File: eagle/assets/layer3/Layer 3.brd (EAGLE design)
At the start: 196 x 158 mm, 84 parts, among them Q2 AO3402, X1 SM06B-SRSS-TB, Y1 8MHz

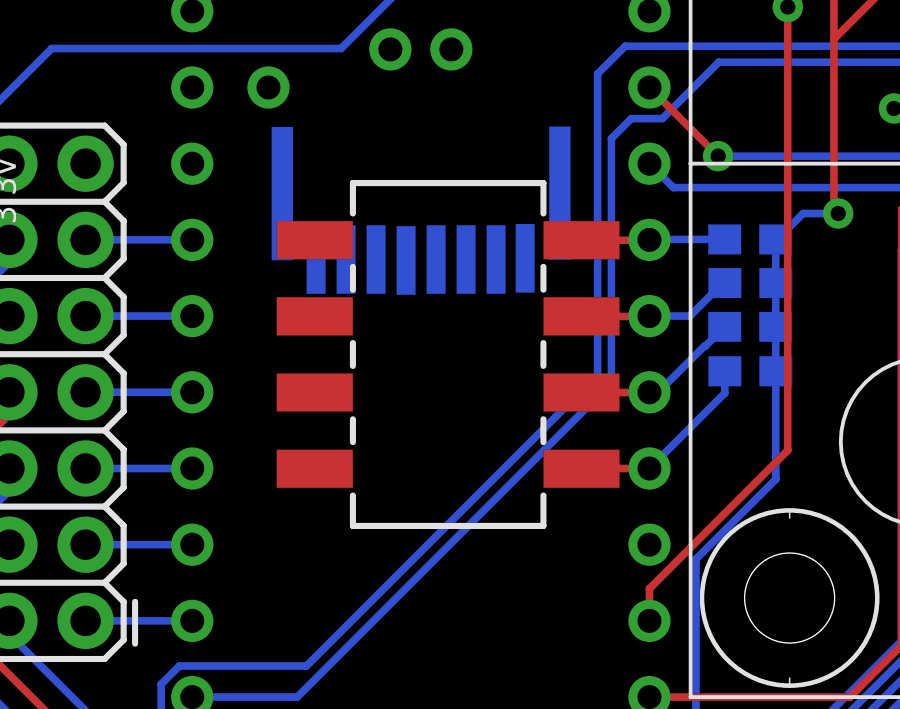
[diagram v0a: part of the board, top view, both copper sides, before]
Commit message: added teensy 4 lbr
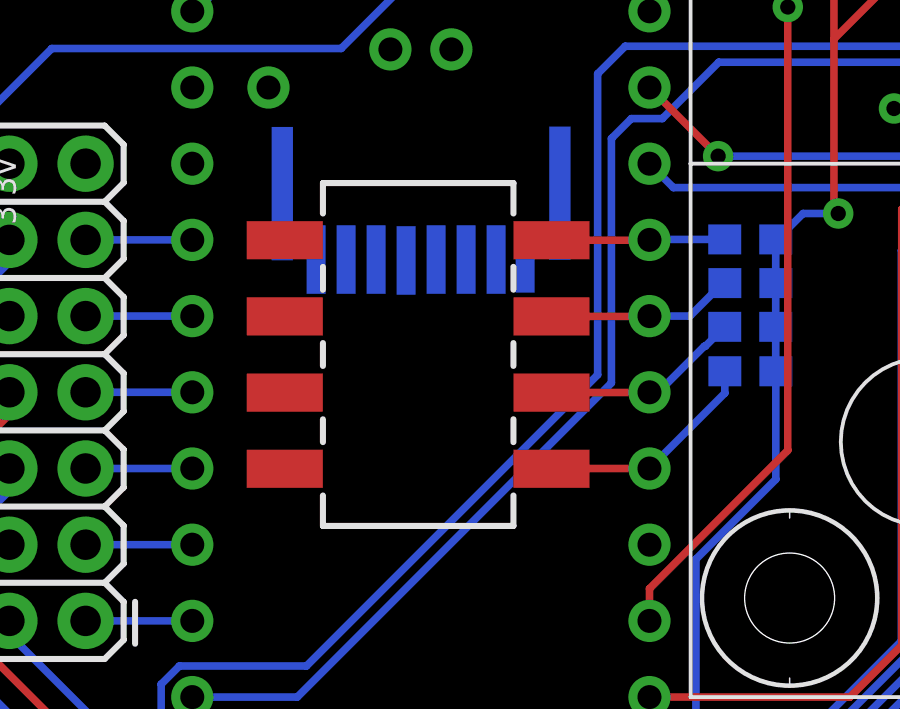
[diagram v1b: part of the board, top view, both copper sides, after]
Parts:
- moved S1 1.00 mm to (-26.9, 3.80)
- renumbered U$1 to TEENSY4
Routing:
- net DIP4: track 6.55 -> 7.55 mm
- net DIP3: track 5.68 -> 6.68 mm
- net DIP2: track 5.24 -> 6.24 mm
- net DIP1: track 4.78 -> 5.78 mm

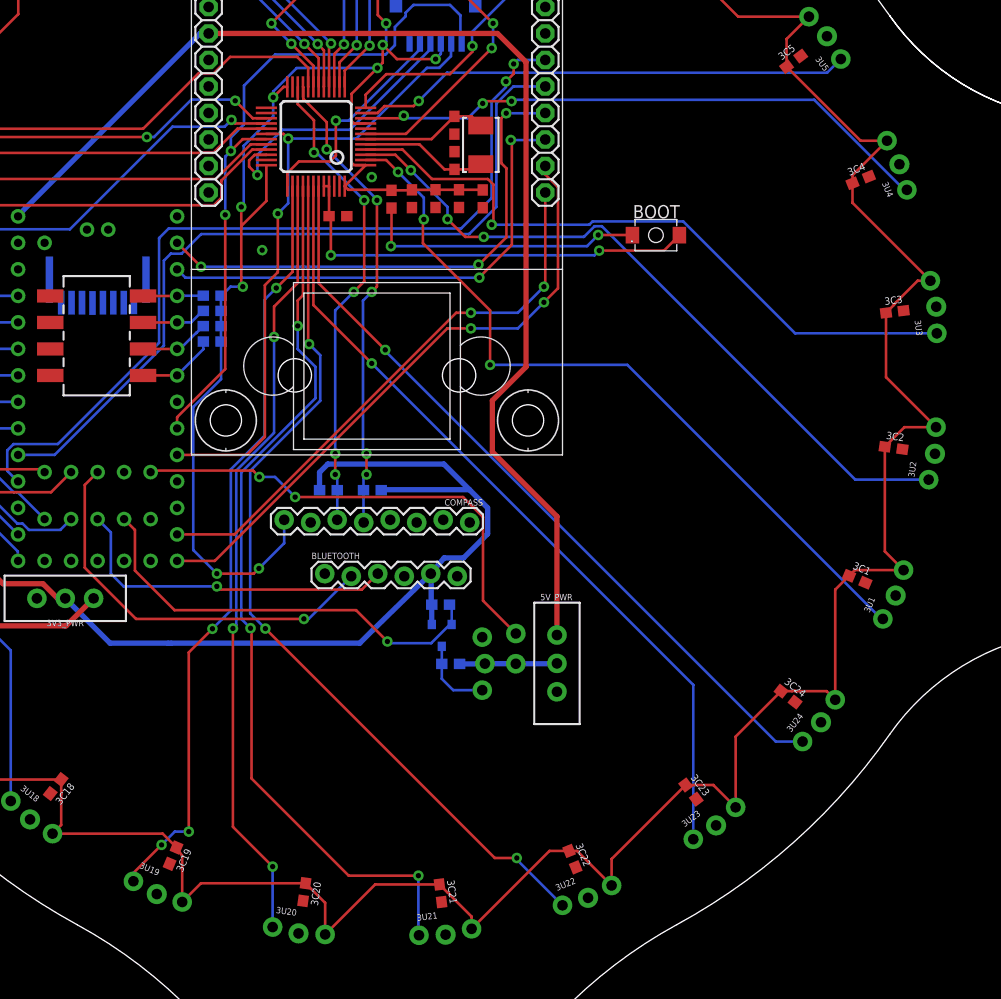
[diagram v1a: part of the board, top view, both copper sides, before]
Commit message: added teensy 4 lbr
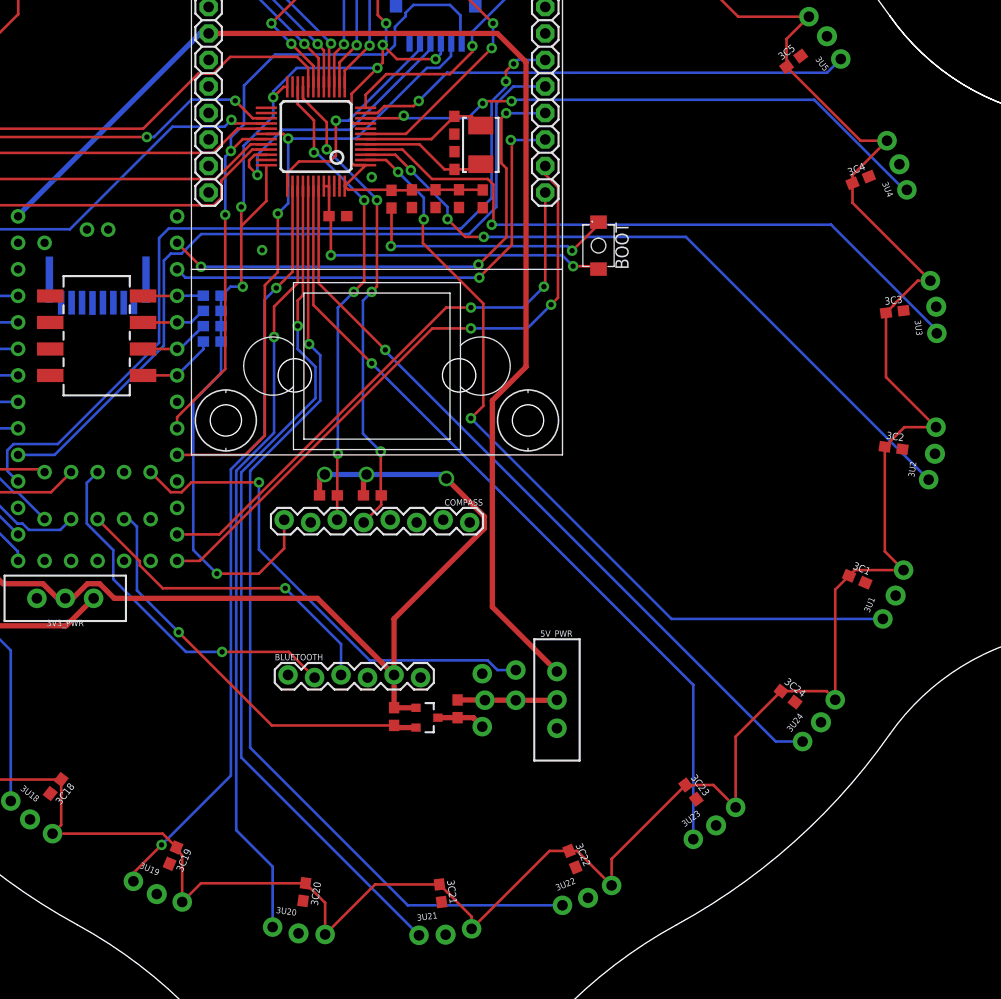
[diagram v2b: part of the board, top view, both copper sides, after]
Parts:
- moved R13 11.6 mm to (1.64, -32.7), flipped to the top, turned to 270 degrees
- moved BLUETOOTH 10.3 mm to (-8.52, -28.7)
- moved Q2 8.07 mm to (4.74, -32.8), flipped to the top, turned to 270 degrees
- moved BOOT 5.59 mm to (21.2, 12.4), turned to 270 degrees
- moved R12 4.36 mm to (7.73, -32.0), flipped to the top, turned to 270 degrees
- moved 5V_PWR 3.50 mm to (17.2, -31.1)
- moved J1 3.50 mm to (13.3, -28.4)
- moved SERVO_IO 3.50 mm to (10.2, -28.6)
- moved R10 0.50 mm to (-4.65, -11.5), flipped to the top, turned to 180 degrees
- moved R11 0.50 mm to (-0.44, -11.5), flipped to the top
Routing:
- net BOOT0: track 41.4 -> 33.4 mm
- net IR22: track 85.8 -> 93.3 mm, vias 3 -> 1
- net IR1: track 73.5 -> 78.6 mm
- net RX_BT: track 38.9 -> 34.9 mm
- net IR21: track 86.6 -> 82.7 mm, vias 3 -> 1
- net 5V_SWITCH: track 115.9 -> 119.4 mm
- net SERVO_HV: track 7.44 -> 4.61 mm
- net N$72: track 27.3 -> 25.0 mm
- net SERVO_LV: track 41.3 -> 39.8 mm
- net 3.3V: track 123.4 -> 122.0 mm, vias 0 -> 3
- net ESC_LV: track 46.2 -> 47.4 mm, vias 2 -> 1
- net SCL1: track 45.5 -> 46.7 mm, vias 5 -> 4
- net TX_BT: track 32.6 -> 31.5 mm
- net IR2: track 68.4 -> 67.5 mm
- net IR19: track 73.7 -> 72.9 mm, vias 4 -> 2
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
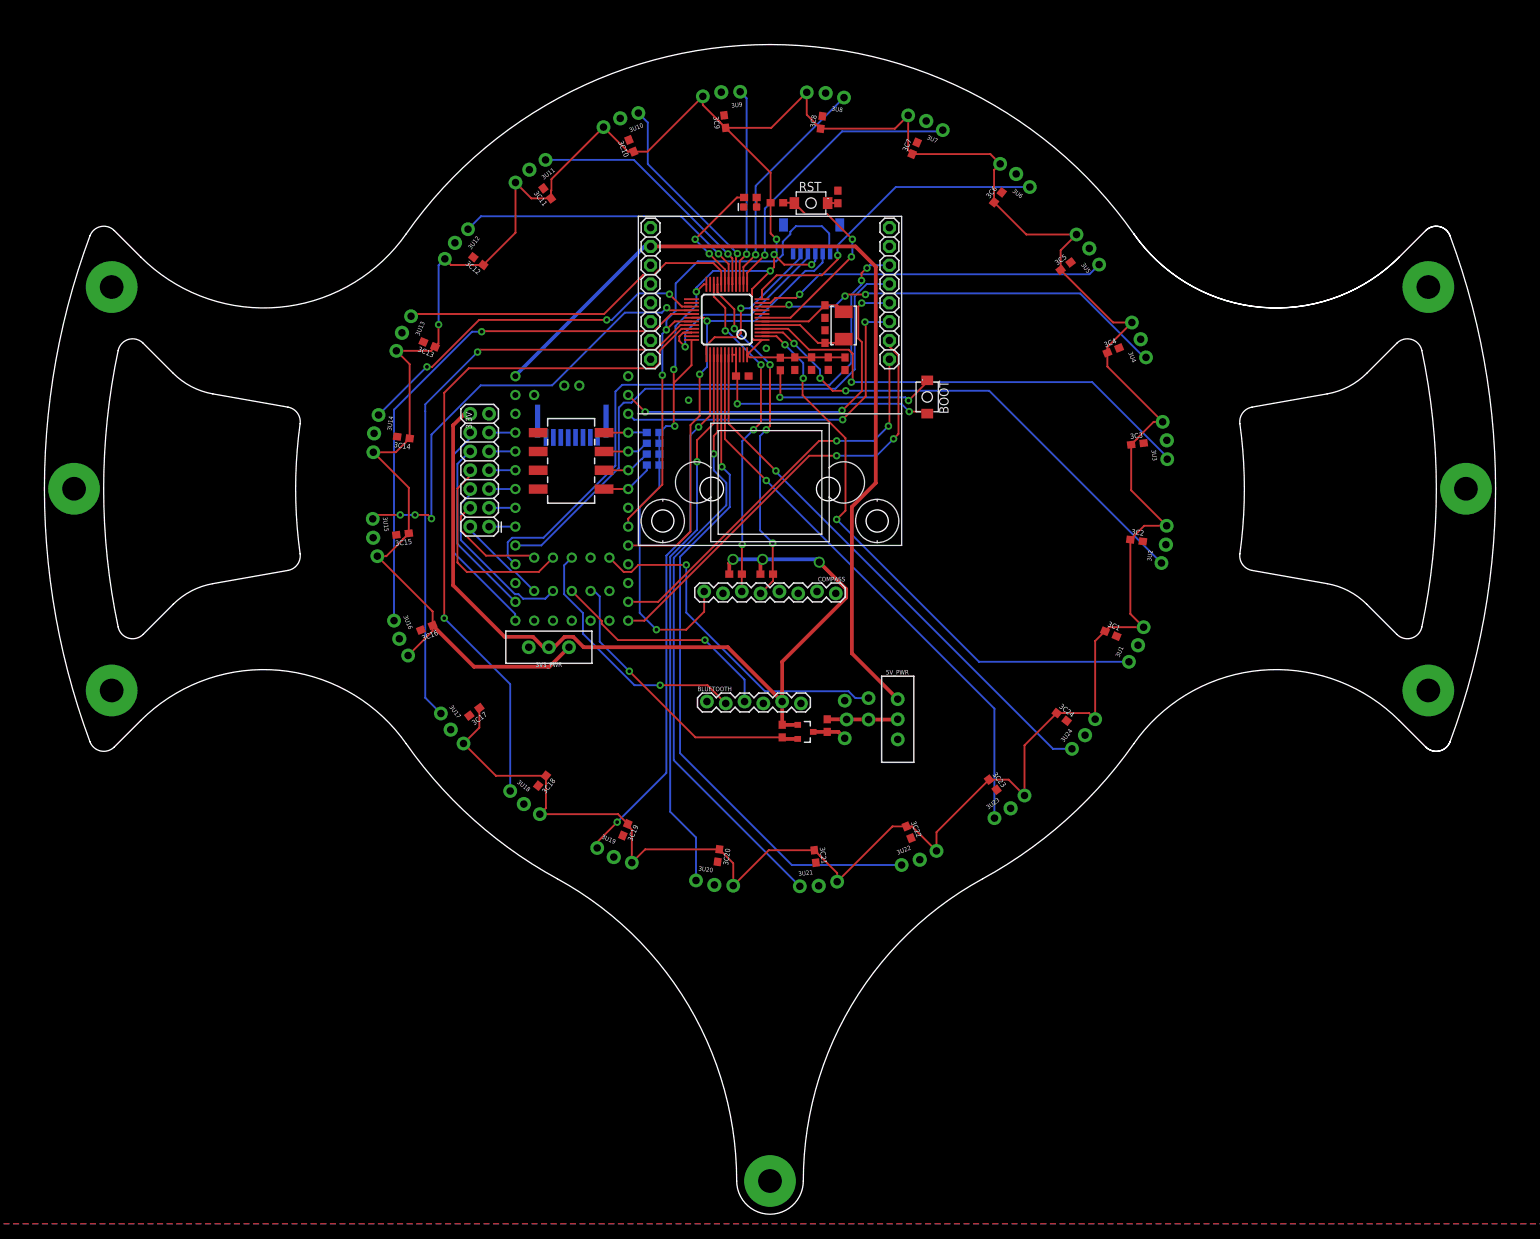
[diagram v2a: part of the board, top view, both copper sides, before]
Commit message: cut more holes beech
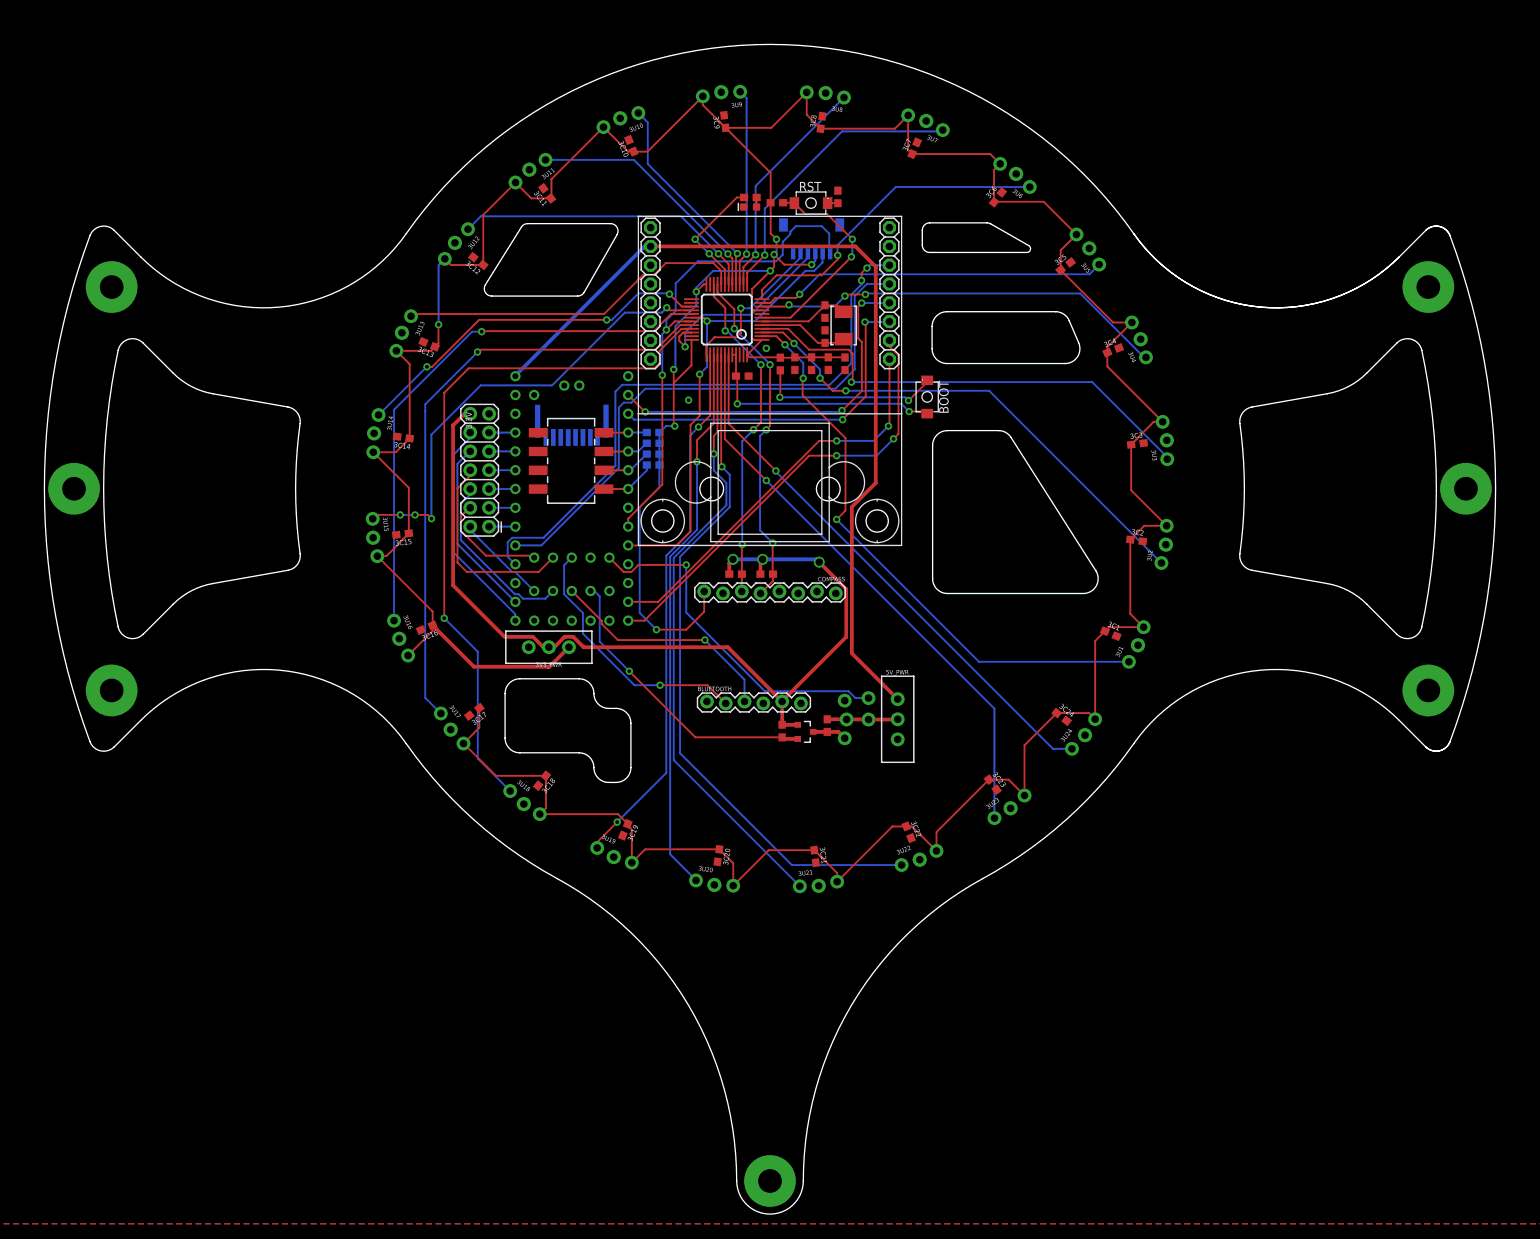
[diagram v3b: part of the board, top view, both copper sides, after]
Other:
- outline, holes or cut-outs redrawn

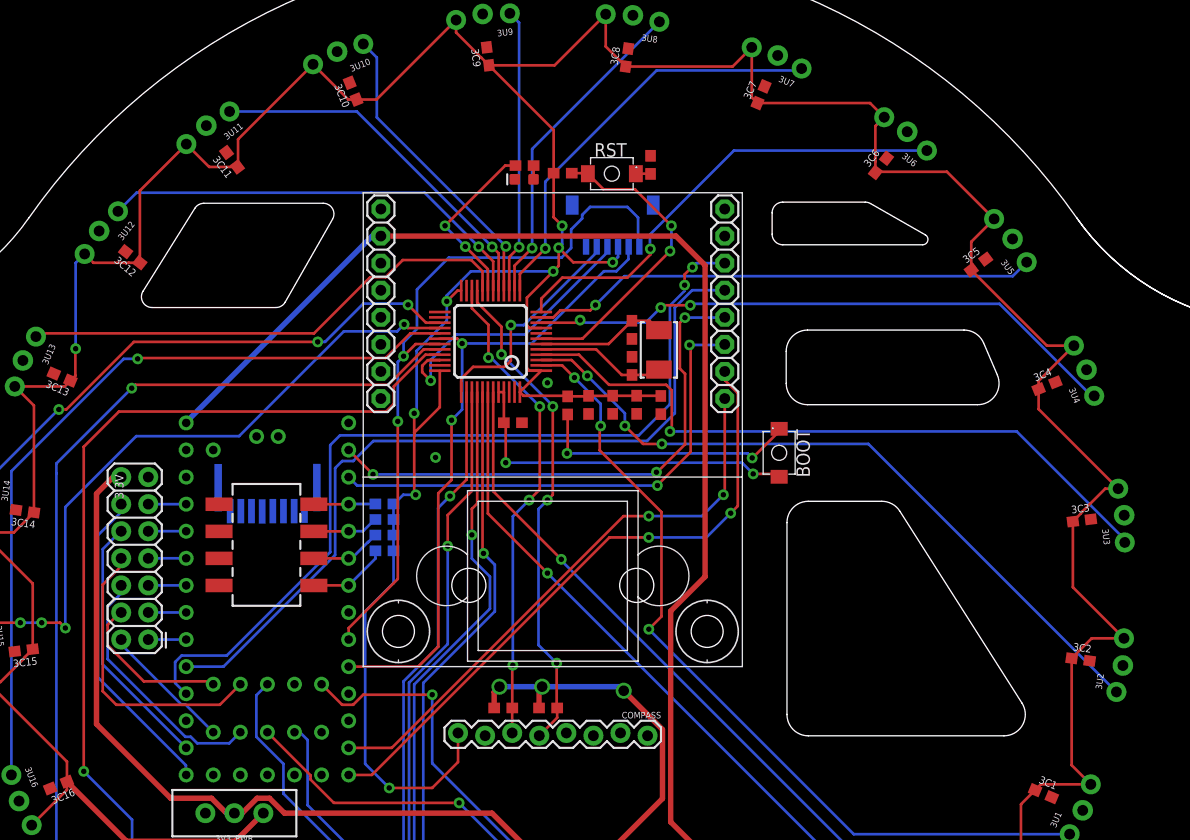
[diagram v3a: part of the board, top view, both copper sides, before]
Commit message: Edited teensy 4 pin out
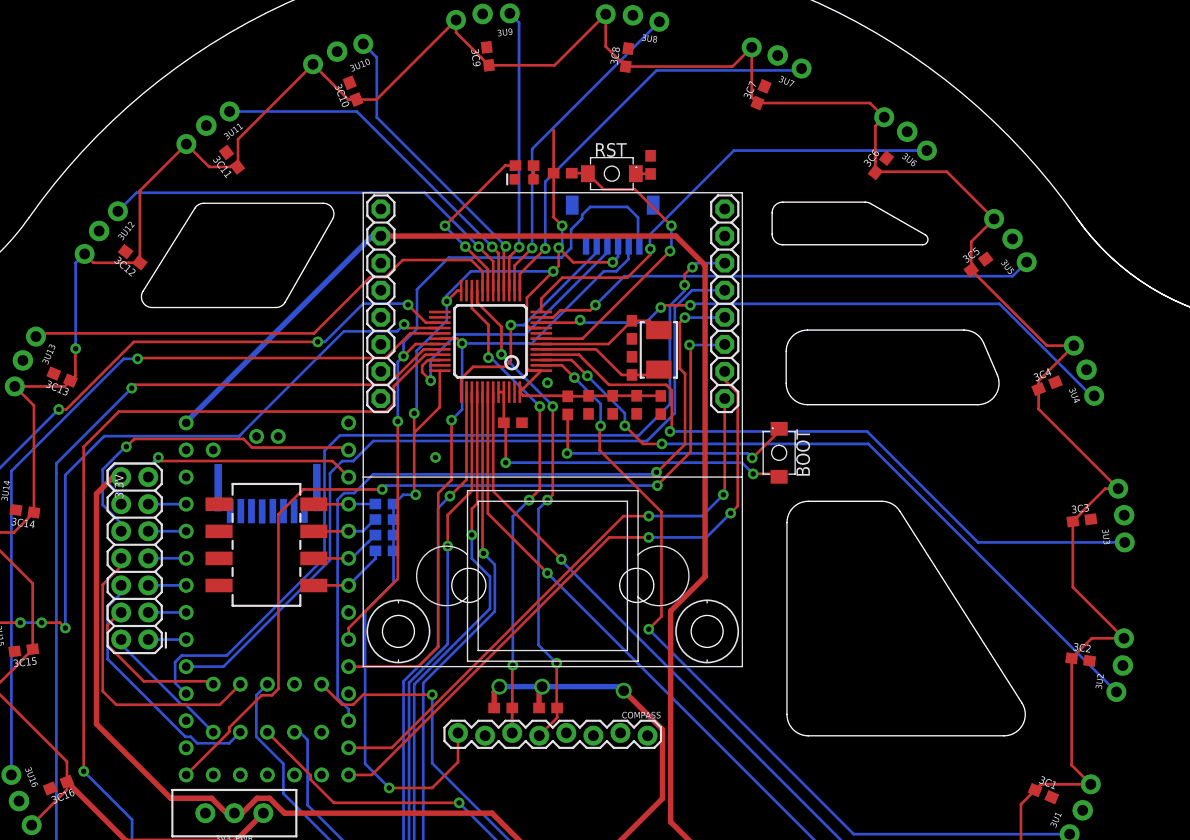
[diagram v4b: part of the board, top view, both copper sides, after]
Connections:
- net RX3_ST1: now also TEENSY4.D0; no longer TEENSY4.D14/A0
- net SCK: now also TEENSY4.D13/LED; no longer TEENSY4.D1
- net SS: now also TEENSY4.D10; no longer TEENSY4.D0
- net TX3_ST1: now also TEENSY4.D1; no longer TEENSY4.D13/LED
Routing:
- net SCK: track 47.1 -> 83.1 mm, vias 2 -> 3
- net SS: track 49.7 -> 72.0 mm, vias 3 -> 2
- net 3V3_SWITCH: track 586.1 -> 577.5 mm
- net RX3_ST1: track 24.3 -> 31.2 mm, vias 0 -> 1
- net TX3_ST1: track 29.7 -> 27.5 mm, vias 0 -> 1
- net IR15: track 62.1 -> 63.8 mm
